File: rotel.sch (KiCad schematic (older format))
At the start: 48 parts

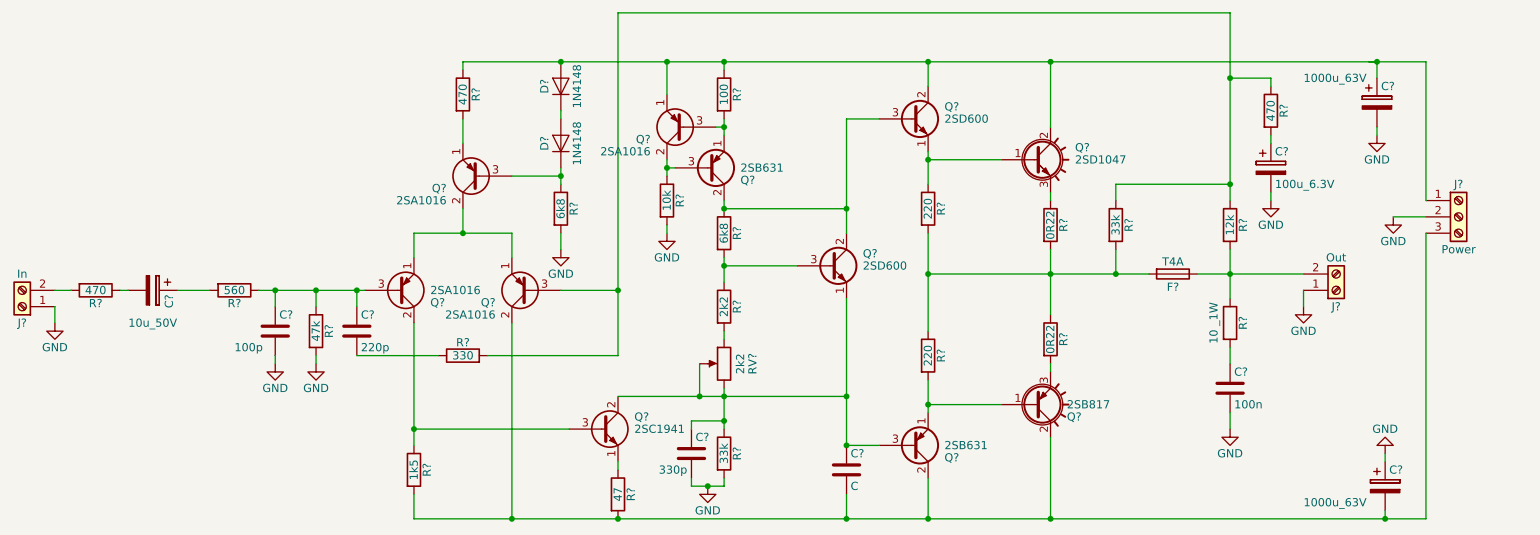
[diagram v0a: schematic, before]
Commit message: added footprints (not double checked).
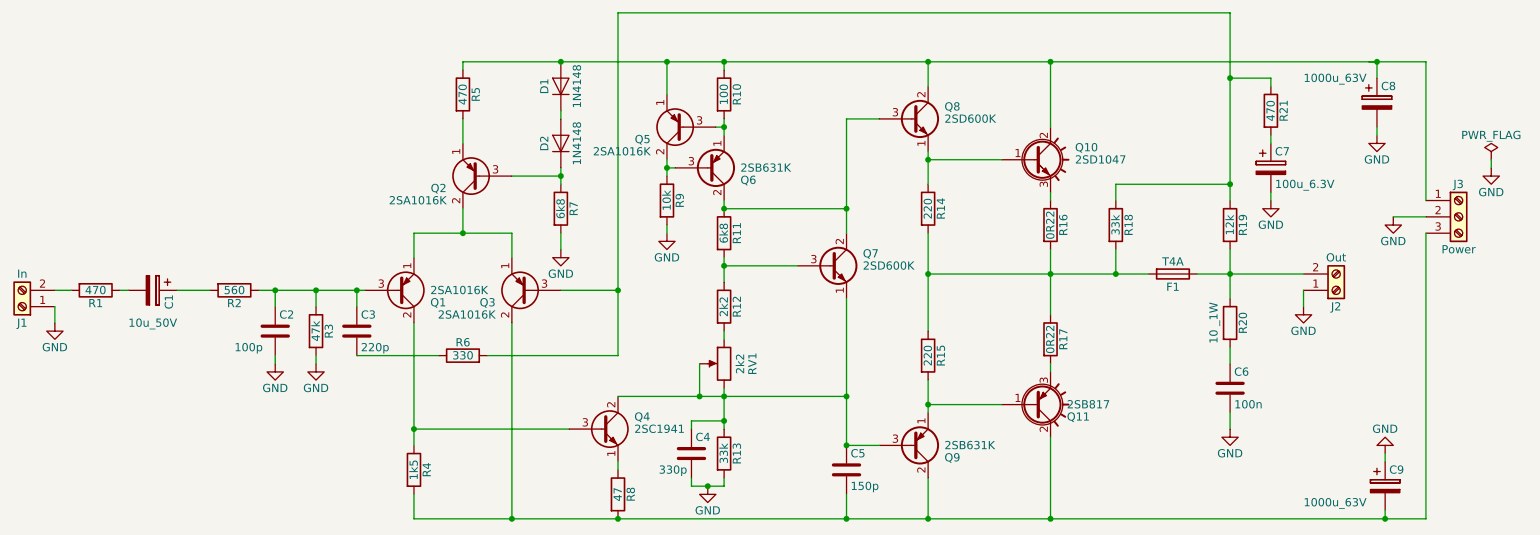
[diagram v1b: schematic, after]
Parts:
- C1, C7: renamed from C?; footprint (none) -> Capacitors_THT:CP_Radial_D8.0mm_P3.80mm
- C2, C3, C4, C6: renamed from C?; footprint (none) -> Capacitors_THT:C_Rect_L7.0mm_W2.5mm_P5.00mm
- C5: renamed from C?; value C -> 150p; footprint (none) -> Capacitors_THT:C_Rect_L7.0mm_W2.5mm_P5.00mm
- C8, C9: renamed from C?; footprint (none) -> Capacitors_THT:CP_Radial_D18.0mm_P7.50mm
- F1: renamed from F?; footprint (none) -> Fuse_Holders_and_Fuses:Fuseholder5x20_horiz_SemiClosed_Casing10x25mm
- J1, J2: renamed from J?; footprint (none) -> TerminalBlock_Phoenix:TerminalBlock_Phoenix_MKDS1.5-2pol
- J3: renamed from J?; footprint (none) -> TerminalBlock_Phoenix:TerminalBlock_Phoenix_MKDS1.5-3pol
- Q1, Q2, Q3, Q5: renamed from Q?; value 2SA1016 -> 2SA1016K
- Q6, Q9: renamed from Q?; value 2SB631 -> 2SB631K
- Q7, Q8: renamed from Q?; value 2SD600 -> 2SD600K
- R1, R10, R11, R12, R13, R14, R15, R18, R19, R2, R21, R3, R4, R5, R6, R7, R8, R9: renamed from R?; footprint (none) -> Resistors_THT:R_Axial_DIN0207_L6.3mm_D2.5mm_P10.16mm_Horizontal
- R16, R17: renamed from R?; footprint (none) -> Resistors_THT:R_Axial_Power_L20.0mm_W6.4mm_P7.62mm_Vertical
- R20: renamed from R?; footprint (none) -> Resistors_THT:R_Axial_DIN0411_L9.9mm_D3.6mm_P15.24mm_Horizontal
- RV1: renamed from RV?; footprint (none) -> Potentiometers:Potentiometer_Trimmer_ACP_CA9v_Horizontal_Px10.0mm_Py5.0mm
- gave numbers to parts that had none: 5

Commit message: Corrected missing footprints
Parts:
- D1, D2: footprint Diodes_THT:D_DO-35_SOD27_Horizontal_RM10 -> Diodes_THT:D_DO-35_SOD27_P10.16mm_Horizontal
- Q10, Q11: footprint TO_SOT_Packages_THT:TO-3PB_Vertical -> TO_SOT_Packages_THT:TO-247_TO-3P_Vertical
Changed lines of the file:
@@
 F 0 "D2" H 4450 2900 50  0000 C CNN
 F 1 "1N4148" H 4450 2700 50  0000 C CNN
-F 2 "Diodes_THT:D_DO-35_SOD27_Horizontal_RM10" H 4450 2625 50  0001 C CNN
+F 2 "Diodes_THT:D_DO-35_SOD27_P10.16mm_Horizontal" H 4450 2625 50  0001 C CNN
 F 3 "" H 4450 2800 50  0001 C CNN
 	1    4450 2800
@@
 F 0 "D1" H 4450 2550 50  0000 C CNN
 F 1 "1N4148" H 4450 2350 50  0000 C CNN
-F 2 "Diodes_THT:D_DO-35_SOD27_Horizontal_RM10" H 4450 2275 50  0001 C CNN
+F 2 "Diodes_THT:D_DO-35_SOD27_P10.16mm_Horizontal" H 4450 2275 50  0001 C CNN
 F 3 "" H 4450 2450 50  0001 C CNN
 	1    4450 2450
@@
 F 0 "Q11" H 7550 4475 50  0000 L CNN
 F 1 "2SB817" H 7550 4400 50  0000 L CNN
-F 2 "TO_SOT_Packages_THT:TO-3PB_Vertical" H 7550 4325 50  0001 L CIN
+F 2 "TO_SOT_Packages_THT:TO-247_TO-3P_Vertical" H 7550 4325 50  0001 L CIN
 F 3 "" H 7350 4400 50  0001 L CNN
 	1    7350 4400
@@
 F 0 "Q10" H 7600 2975 50  0000 L CNN
 F 1 "2SD1047" H 7600 2900 50  0000 L CNN
-F 2 "TO_SOT_Packages_THT:TO-3PB_Vertical" H 7600 2825 50  0001 L CIN
+F 2 "TO_SOT_Packages_THT:TO-247_TO-3P_Vertical" H 7600 2825 50  0001 L CIN
 F 3 "" H 7350 2900 50  0001 L CNN
 	1    7350 2900

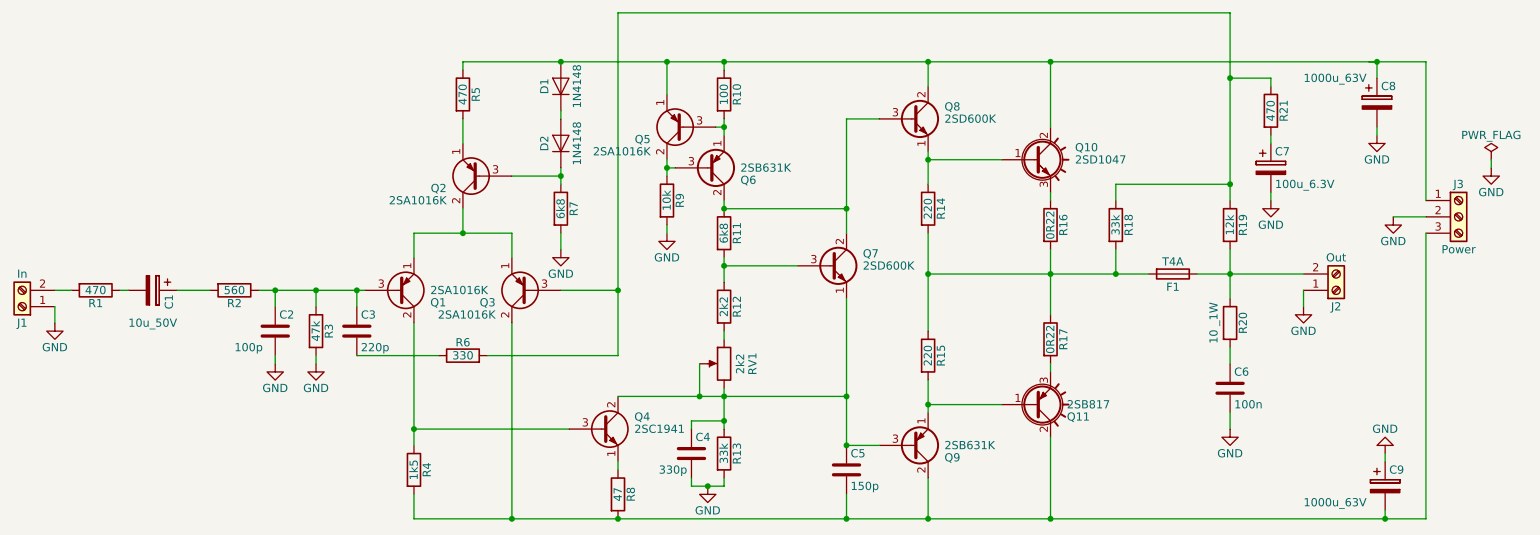
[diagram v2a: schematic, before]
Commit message: First PCB version. No silkscreen.
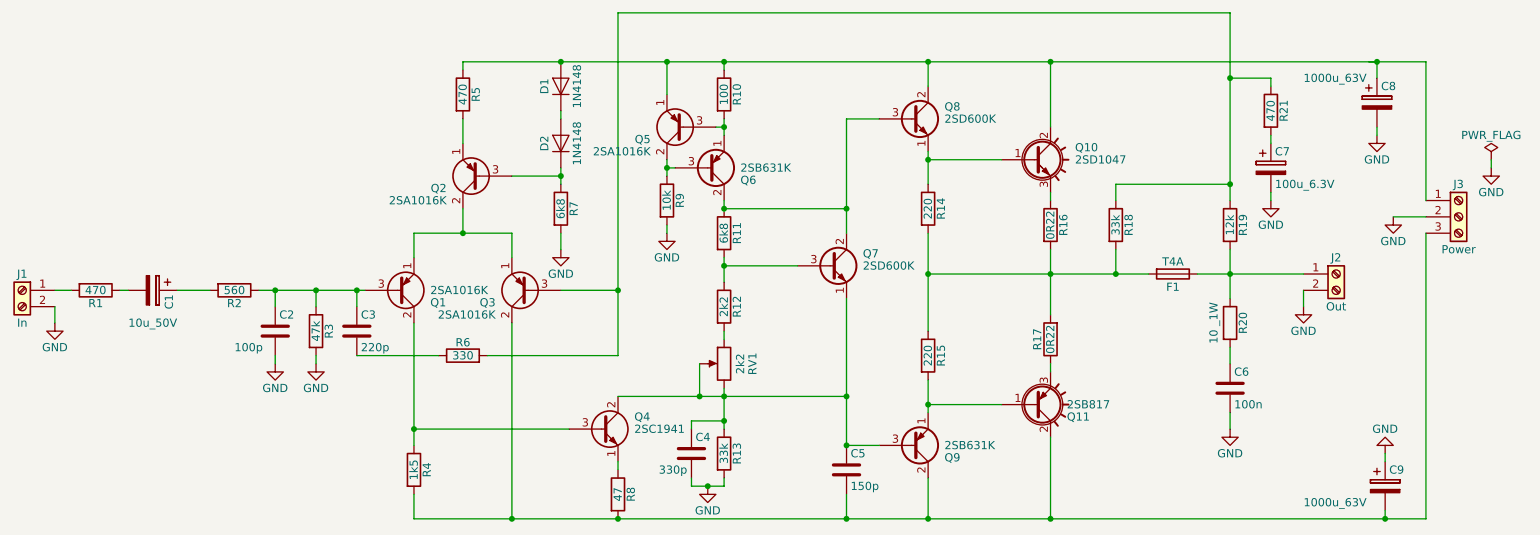
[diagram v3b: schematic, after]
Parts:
- Q1, Q2, Q3, Q4, Q5: footprint TO_SOT_Packages_THT:TO-92_Molded_Narrow -> TO_SOT_Packages_THT:TO-92_Inline_Narrow_Oval
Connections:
- net GND: now also J1.2 (Pin_2), J2.2 (Pin_2); no longer J1.1 (Pin_1), J2.1 (Pin_1)
- net at R1.2: now also J1.1 (Pin_1); no longer J1.2 (Pin_2)
- net at F1.2, R14.2, R15.1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: now also R17.2; no longer R17.1
- net at Q11.3 (E): now also R17.1; no longer R17.2
- net at F1.1, R19.2, R20.1: now also J2.1 (Pin_1); no longer J2.2 (Pin_2)
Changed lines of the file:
@@
 F 0 "Q1" H 3650 3775 50  0000 L CNN
 F 1 "2SA1016K" H 3650 3700 50  0000 L CNN
-F 2 "TO_SOT_Packages_THT:TO-92_Molded_Narrow" H 3650 3625 50  0001 L CIN
+F 2 "TO_SOT_Packages_THT:TO-92_Inline_Narrow_Oval" H 3650 3625 50  0001 L CIN
 F 3 "" H 3450 3700 50  0001 L CNN
 	1    3450 3700
@@
 F 0 "Q3" H 4450 3775 50  0000 L CNN
 F 1 "2SA1016K" H 4450 3850 50  0000 L CNN
-F 2 "TO_SOT_Packages_THT:TO-92_Molded_Narrow" H 4450 3625 50  0001 L CIN
+F 2 "TO_SOT_Packages_THT:TO-92_Inline_Narrow_Oval" H 4450 3625 50  0001 L CIN
 F 3 "" H 4250 3700 50  0001 L CNN
 	1    4250 3700
@@
 F 0 "Q2" H 4150 3075 50  0000 L CNN
 F 1 "2SA1016K" H 4150 3150 50  0000 L CNN
-F 2 "TO_SOT_Packages_THT:TO-92_Molded_Narrow" H 4150 2925 50  0001 L CIN
+F 2 "TO_SOT_Packages_THT:TO-92_Inline_Narrow_Oval" H 4150 2925 50  0001 L CIN
 F 3 "" H 3950 3000 50  0001 L CNN
 	1    3950 3000
@@
 F 0 "Q5" H 5400 2775 50  0000 L CNN
 F 1 "2SA1016K" H 5400 2850 50  0000 L CNN
-F 2 "TO_SOT_Packages_THT:TO-92_Molded_Narrow" H 5400 2625 50  0001 L CIN
+F 2 "TO_SOT_Packages_THT:TO-92_Inline_Narrow_Oval" H 5400 2625 50  0001 L CIN
 F 3 "" H 5200 2700 50  0001 L CNN
 	1    5200 2700
@@
 F 0 "Q4" H 4900 4625 50  0000 L CNN
 F 1 "2SC1941" H 4900 4550 50  0000 L CNN
-F 2 "TO_SOT_Packages_THT:TO-92_Molded_Narrow" H 4900 4475 50  0001 L CIN
+F 2 "TO_SOT_Packages_THT:TO-92_Inline_Narrow_Oval" H 4900 4475 50  0001 L CIN
 F 3 "" H 4700 4550 50  0001 L CNN
 	1    4700 4550
@@
 F 3 "" H 7450 4000 50  0001 C CNN
 	1    7450 4000
-	1    0    0    -1
+	-1   0    0    1
 $EndComp
 $Comp
@@
 L Screw_Terminal_01x02 J1
 U 1 1 5E7C841E
-P 1150 3800
-F 0 "J1" H 1150 3900 50  0000 C CNN
-F 1 "In" H 1150 3600 50  0000 C CNN
-F 2 "TerminalBlock_Phoenix:TerminalBlock_Phoenix_MKDS1.5-2pol" H 1150 3800 50  0001 C CNN
-F 3 "" H 1150 3800 50  0001 C CNN
-	1    1150 3800
-	-1   0    0    1
+P 1150 3700
+F 0 "J1" H 1150 3800 50  0000 C CNN
+F 1 "In" H 1150 3500 50  0000 C CNN
+F 2 "TerminalBlock_Phoenix:TerminalBlock_Phoenix_MKDS1.5-2pol" H 1150 3700 50  0001 C CNN
+F 3 "" H 1150 3700 50  0001 C CNN
+	1    1150 3700
+	-1   0    0    -1
 $EndComp
 $Comp
@@
 L Screw_Terminal_01x02 J2
 U 1 1 5E7C92CD
-P 9200 3700
-F 0 "J2" H 9200 3800 50  0000 C CNN
-F 1 "Out" H 9200 3500 50  0000 C CNN
-F 2 "TerminalBlock_Phoenix:TerminalBlock_Phoenix_MKDS1.5-2pol" H 9200 3700 50  0001 C CNN
-F 3 "" H 9200 3700 50  0001 C CNN
-	1    9200 3700
-	1    0    0    1
-$EndComp
-$Comp
+P 9200 3600
+F 0 "J2" H 9200 3700 50  0000 C CNN
+F 1 "Out" H 9200 3400 50  0000 C CNN
+F 2 "TerminalBlock_Phoenix:TerminalBlock_Phoenix_MKDS1.5-2pol" H 9200 3600 50  0001 C CNN
+F 3 "" H 9200 3600 50  0001 C CNN
+	1    9200 3600
+	1    0    0    -1
+$EndComp
+$Comp
